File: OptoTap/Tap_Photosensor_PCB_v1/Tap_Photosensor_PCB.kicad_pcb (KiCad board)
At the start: 2 copper layers, 28.8 x 10.2 mm, 11 parts, among them J1 Conn_01x01_Male, J2 Conn_01x01_Male, J3 Conn_01x01_Male, U1 OPB961N51

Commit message: updated kicad files with proper resistor values
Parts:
- R1: value R1K -> 1K
- R2: value R200 -> 200R
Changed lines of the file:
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@@
       (effects (font (size 0.7 0.7) (thickness 0.1)))
     )
-    (fp_text value "R200" (at 0 1.65 90) (layer "F.Fab")
+    (fp_text value "200R" (at 0 1.65 90) (layer "F.Fab")
       (effects (font (size 1 1) (thickness 0.15)))
     )
@@
       (effects (font (size 0.7 0.7) (thickness 0.1)))
     )
-    (fp_text value "R1K" (at 0 1.65 90) (layer "F.Fab")
+    (fp_text value "1K" (at 0 1.65 90) (layer "F.Fab")
       (effects (font (size 1 1) (thickness 0.15)))
     )
@@
     (property "Sheetname" "")
     (attr through_hole exclude_from_pos_files exclude_from_bom)
-    (fp_text reference "U1" (at -0.1 2.275 180) (layer "B.SilkS")
+    (fp_text reference "U1" (at -0.1 1.95 180) (layer "B.SilkS")
       (effects (font (size 1.4 1.4) (thickness 0.15)) (justify mirror))
     )
@@
     (fp_line (start 6.16 3.175) (end 6.16 -3.175) (layer "B.SilkS") (width 0.127))
     (fp_line (start -6.16 3.175) (end 6.16 3.175) (layer "B.SilkS") (width 0.127))
+    (fp_line (start -6.16 -3.175) (end -6.16 3.175) (layer "B.SilkS") (width 0.127))
     (fp_line (start 6.16 -3.175) (end -6.16 -3.175) (layer "B.SilkS") (width 0.127))
-    (fp_line (start -6.16 -3.175) (end -6.16 3.175) (layer "B.SilkS") (width 0.127))
     (fp_circle (center -6.61 1.27) (end -6.51 1.27) (layer "B.SilkS") (width 0.2) (fill none))
+    (fp_line (start 6.41 -3.425) (end -6.41 -3.425) (layer "B.CrtYd") (width 0.05))
+    (fp_line (start -6.41 3.425) (end 6.41 3.425) (layer "B.CrtYd") (width 0.05))
     (fp_line (start 6.41 3.425) (end 6.41 -3.425) (layer "B.CrtYd") (width 0.05))
-    (fp_line (start -6.41 3.425) (end 6.41 3.425) (layer "B.CrtYd") (width 0.05))
-    (fp_line (start 6.41 -3.425) (end -6.41 -3.425) (layer "B.CrtYd") (width 0.05))
     (fp_line (start -6.41 -3.425) (end -6.41 3.425) (layer "B.CrtYd") (width 0.05))
-    (fp_line (start -6.16 3.175) (end 6.16 3.175) (layer "B.Fab") (width 0.127))
+    (fp_line (start -6.16 -3.175) (end -6.16 3.175) (layer "B.Fab") (width 0.127))
     (fp_line (start 6.16 3.175) (end 6.16 -3.175) (layer "B.Fab") (width 0.127))
     (fp_line (start 6.16 -3.175) (end -6.16 -3.175) (layer "B.Fab") (width 0.127))
-    (fp_line (start -6.16 -3.175) (end -6.16 3.175) (layer "B.Fab") (width 0.127))
+    (fp_line (start -6.16 3.175) (end 6.16 3.175) (layer "B.Fab") (width 0.127))
     (fp_circle (center -6.61 1.27) (end -6.51 1.27) (layer "B.Fab") (width 0.2) (fill none))
     (pad "1" thru_hole rect locked (at -4.065 1.27) (size 1.31 1.31) (drill 0.87) (layers *.Cu *.Mask)

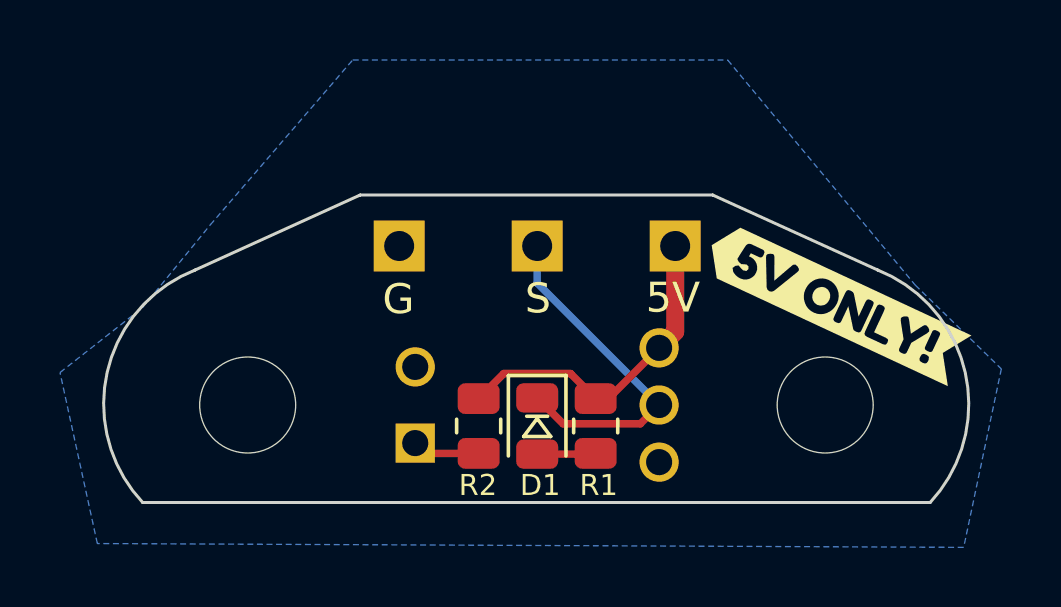
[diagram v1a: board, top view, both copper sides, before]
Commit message: updated OptoTap boards (#53)
* updated OptoTap boards

* changed footprint text to specify EE-SX398

* added solder jig step

* fixed link
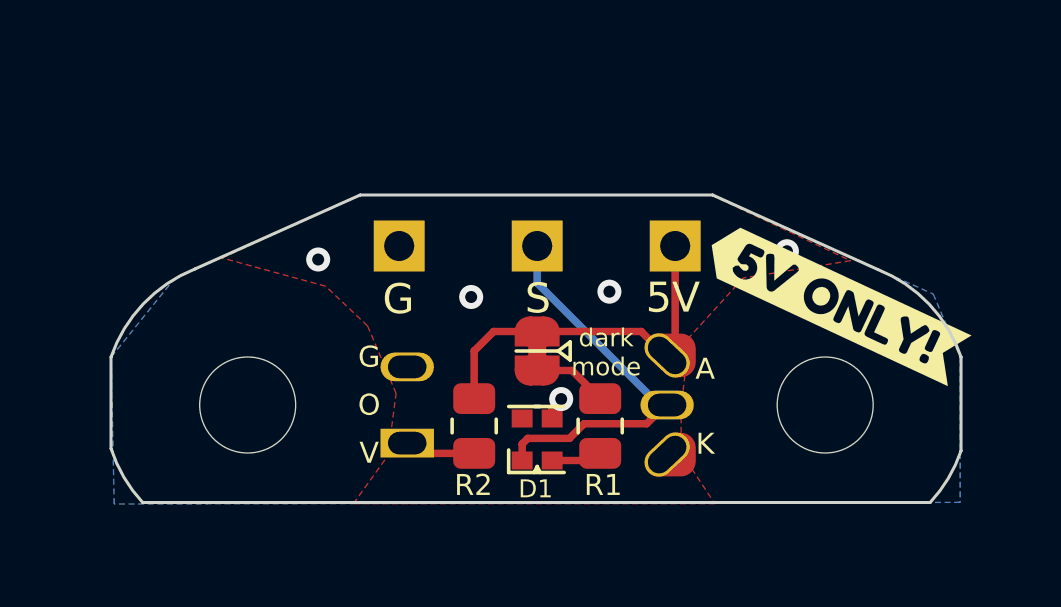
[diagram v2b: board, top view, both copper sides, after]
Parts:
- added JP1: SolderJumper_2_Bridged, Jumper:SolderJumper-2_P1.3mm_Bridged_RoundedPad1.0x1.5mm, F.Cu at (112.4, 63.7)
- D1: value LED -> XL-1615RGBC; footprint LED_SMD:LED_0805_2012Metric -> LED_SMD:LED_0606_1432
- U1: value OPB961N51 -> OPB961N5/EE-SX398; footprint footprints:OPTO_OPB961N51 -> footprints:OPTO_EE-SX398_OPB666N
- moved D1 0.45 mm to (112.4, 66.7), turned to 90 degrees
- moved R1 0.15 mm to (114.5, 66.2)
- moved R2 0.15 mm to (110.3, 66.2)
- turned U1 to 180 degrees
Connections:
- R1 pad 1: +5V -> Net-(JP1-Pad1)
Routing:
- net Net-(JP1-Pad1): track 0.00 -> 2.49 mm
- net +5V: track 11.0 -> 12.5 mm
- net SIG: track 11.7 -> 12.8 mm
- net GND: track 0.00 -> 0.77 mm, vias 0 -> 5
- added copper zone on F.Cu, net GND
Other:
- board size 28.8 x 10.2 mm -> 28.3 x 10.2 mm
- board text added: "dark mode"
- board text added: "rev 1.3"
- board text removed: "OPB666N OPB971"
- board text removed: "rev 1.0"

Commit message: Opto24 (#68)
* updated OptoTap boards

* updated inductor info

* updated STEP and kicad

* updated README with LED ordering info

* fixed bad save
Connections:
- net Net-(D1-Pad2) renamed /LED+
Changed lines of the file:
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@@
   (net 2 "+5V")
   (net 3 "GND")
-  (net 4 "Net-(D1-Pad2)")
-  (net 5 "unconnected-(D1-Pad4)")
-  (net 6 "Net-(R2-Pad2)")
-  (net 7 "Net-(JP1-Pad1)")
+  (net 4 "/LED+")
+  (net 5 "unconnected-(D1-G-Pad4)")
+  (net 6 "Net-(JP1-A)")
+  (net 7 "Net-(U1-A)")
   (footprint "Jumper:SolderJumper-2_P1.3mm_Bridged_RoundedPad1.0x1.5mm" (layer "F.Cu")
     (at 112.4 63.7 90)
@@
     (property "Sheetfile" "Tap_Photosensor_PCB.kicad_sch")
     (property "Sheetname" "")
-    (attr exclude_from_pos_files exclude_from_bom)
+    (property "ki_description" "Solder Jumper, 2-pole, closed/bridged")
+    (property "ki_keywords" "solder jumper SPST")
+    (attr exclude_from_pos_files)
     (net_tie_pad_groups "1, 2")
     (fp_text reference "JP1" (at 0 -2.15 90) (layer "F.SilkS") hide
@@
       (stroke (width 0.12) (type solid)) (layer "F.SilkS"))
     (pad "1" smd custom (at -0.65 0 90) (size 1 0.5) (layers "F.Cu" "F.Mask")
-      (net 7 "Net-(JP1-Pad1)") (pinfunction "A") (pintype "passive") (zone_connect 2) (thermal_bridge_angle 45)
+      (net 6 "Net-(JP1-A)") (pinfunction "A") (pintype "passive") (zone_connect 2) (thermal_bridge_angle 45)
       (options (clearance outline) (anchor rect))
       (primitives
@@
     (property "Sheetfile" "Tap_Photosensor_PCB.kicad_sch")
     (property "Sheetname" "")
-    (attr through_hole exclude_from_pos_files exclude_from_bom)
+    (property "ki_description" "Generic connector, single row, 01x01, script generated (kicad-library-utils/schlib/autogen/connector/)")
+    (property "ki_keywords" "connector")
+    (attr through_hole exclude_from_pos_files)
     (fp_text reference "J1" (at 0 -2.33) (layer "F.SilkS") hide
         (effects (font (size 1 1) (thickness 0.15)))
@@
     (property "Sheetfile" "Tap_Photosensor_PCB.kicad_sch")
     (property "Sheetname" "")
+    (property "ki_description" "Resistor")
+    (property "ki_keywords" "R res resistor")
     (attr smd)
     (fp_text reference "R2" (at 1.975 0.025 180) (layer "F.SilkS")
@@
       (net 2 "+5V") (pintype "passive"))
     (pad "2" smd roundrect (at 0.9125 0 270) (size 1.025 1.4) (layers "F.Cu" "F.Paste" "F.Mask") (roundrect_rratio 0.243902439)
-      (net 6 "Net-(R2-Pad2)") (pintype "passive"))
+      (net 7 "Net-(U1-A)") (pintype "passive"))
     (model "${KICAD6_3DMODEL_DIR}/Resistor_SMD.3dshapes/R_0805_2012Metric.wrl"
       (offset (xyz 0 0 0))
@@
     (property "Sheetfile" "Tap_Photosensor_PCB.kicad_sch")
     (property "Sheetname" "")
+    (property "ki_description" "LED RGB, Common Anode, SMD, 3.0x1.5mm, Horizontal")
+    (property "ki_keywords" "LED RGB SMD Kingbright APFA3010 Horizontal")
     (attr smd)
     (fp_text reference "D1" (at -1.65 -0.05 unlocked) (layer "F.SilkS")
@@
       (net 1 "SIG") (pinfunction "R") (pintype "input"))
     (pad "2" smd rect (at -0.7 0.5 90) (size 0.6 0.7) (layers "F.Cu" "F.Paste" "F.Mask")
-      (net 4 "Net-(D1-Pad2)") (pinfunction "A") (pintype "power_in"))
+      (net 4 "/LED+") (pinfunction "A") (pintype "power_in"))
     (pad "3" smd rect (at 0.7 0.5 90) (size 0.6 0.7) (layers "F.Cu" "F.Paste" "F.Mask")
       (net 3 "GND") (pinfunction "B") (pintype "input"))
     (pad "4" smd rect (at 0.7 -0.5 90) (size 0.6 0.7) (layers "F.Cu" "F.Paste" "F.Mask")
-      (net 5 "unconnected-(D1-Pad4)") (pinfunction "G") (pintype "input+no_connect"))
+      (net 5 "unconnected-(D1-G-Pad4)") (pinfunction "G") (pintype "input+no_connect"))
   )
   (footprint "Connector_PinHeader_2.54mm:PinHeader_1x01_P2.54mm_Vertical" (layer "F.Cu")
@@
     (property "Sheetfile" "Tap_Photosensor_PCB.kicad_sch")
     (property "Sheetname" "")
-    (attr through_hole exclude_from_pos_files exclude_from_bom)
+    (property "ki_description" "Generic connector, single row, 01x01, script generated (kicad-library-utils/schlib/autogen/connector/)")
+    (property "ki_keywords" "connector")
+    (attr through_hole exclude_from_pos_files)
     (fp_text reference "J2" (at 0 -2.33) (layer "F.SilkS") hide
         (effects (font (size 1 1) (thickness 0.15)))
@@
     (property "Sheetfile" "Tap_Photosensor_PCB.kicad_sch")
     (property "Sheetname" "")
+    (property "ki_description" "Resistor")
+    (property "ki_keywords" "R res resistor")
     (attr smd)
     (fp_text reference "R1" (at 1.975 -0.1 180) (layer "F.SilkS")
@@
       (stroke (width 0.1) (type solid)) (layer "F.Fab"))
     (pad "1" smd roundrect (at -0.9125 0 270) (size 1.025 1.4) (layers "F.Cu" "F.Paste" "F.Mask") (roundrect_rratio 0.243902439)
-      (net 7 "Net-(JP1-Pad1)") (pintype "passive"))
+      (net 6 "Net-(JP1-A)") (pintype "passive"))
     (pad "2" smd roundrect (at 0.9125 0 270) (size 1.025 1.4) (layers "F.Cu" "F.Paste" "F.Mask") (roundrect_rratio 0.243902439)
-      (net 4 "Net-(D1-Pad2)") (pintype "passive"))
+      (net 4 "/LED+") (pintype "passive"))
     (model "${KICAD6_3DMODEL_DIR}/Resistor_SMD.3dshapes/R_0805_2012Metric.wrl"
       (offset (xyz 0 0 0))
@@
     (property "Sheetfile" "Tap_Photosensor_PCB.kicad_sch")
     (property "Sheetname" "")
-    (attr through_hole exclude_from_pos_files exclude_from_bom)
+    (property "ki_description" "Generic connector, single row, 01x01, script generated (kicad-library-utils/schlib/autogen/connector/)")
+    (property "ki_keywords" "connector")
+    (attr through_hole exclude_from_pos_files)
     (fp_text reference "J3" (at 0 -2.33) (layer "F.SilkS") hide
         (effects (font (size 1 1) (thickness 0.15)))
@@
     (property "Sheetfile" "Tap_Photosensor_PCB.kicad_sch")
     (property "Sheetname" "")
-    (attr through_hole exclude_from_pos_files exclude_from_bom)
+    (attr through_hole exclude_from_pos_files)
     (fp_text reference "U1" (at 0 1.4) (layer "B.SilkS")
         (effects (font (size 1 1) (thickness 0.15)) (justify mirror))
@@
       (stroke (width 0.1) (type solid)) (layer "User.3"))
     (pad "1" thru_hole rect (at 4.332 -1.27) (size 1.782 0.958) (drill oval 1.286 0.758) (layers "*.Cu" "*.Mask")
-      (net 6 "Net-(R2-Pad2)") (pinfunction "A") (pintype "passive"))
+      (net 7 "Net-(U1-A)") (pinfunction "A") (pintype "passive"))
     (pad "2" thru_hole oval (at 4.332 1.27) (size 1.782 0.958) (drill oval 1.286 0.758) (layers "*.Cu" "*.Mask")
       (net 3 "GND") (pinfunction "K") (pintype "passive"))
@@
   (segment (start 114.2625 67.35) (end 114.5 67.1125) (width 0.25) (layer "F.Cu") (net 4))
   (segment (start 112.9 67.35) (end 114.2625 67.35) (width 0.25) (layer "F.Cu") (net 4))
-  (segment (start 108.4305 67.1125) (end 108.068 66.75) (width 0.25) (layer "F.Cu") (net 6))
-  (segment (start 110.3 67.1125) (end 108.4305 67.1125) (width 0.25) (layer "F.Cu") (net 6))
-  (segment (start 113.5625 64.35) (end 114.5 65.2875) (width 0.25) (layer "F.Cu") (net 7))
-  (segment (start 112.4 64.35) (end 113.5625 64.35) (width 0.25) (layer "F.Cu") (net 7))
+  (segment (start 113.5625 64.35) (end 114.5 65.2875) (width 0.25) (layer "F.Cu") (net 6))
+  (segment (start 112.4 64.35) (end 113.5625 64.35) (width 0.25) (layer "F.Cu") (net 6))
+  (segment (start 108.4305 67.1125) (end 108.068 66.75) (width 0.25) (layer "F.Cu") (net 7))
+  (segment (start 110.3 67.1125) (end 108.4305 67.1125) (width 0.25) (layer "F.Cu") (net 7))
   (zone (net 3) (net_name "GND") (layer "F.Cu") (hatch edge 0.508)
     (connect_pads (clearance 0.508))
